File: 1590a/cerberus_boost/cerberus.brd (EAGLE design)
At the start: 33 x 31.7 mm, 30 parts, among them Q1 2N5088, Q2 2N5088, Q3 2N5087

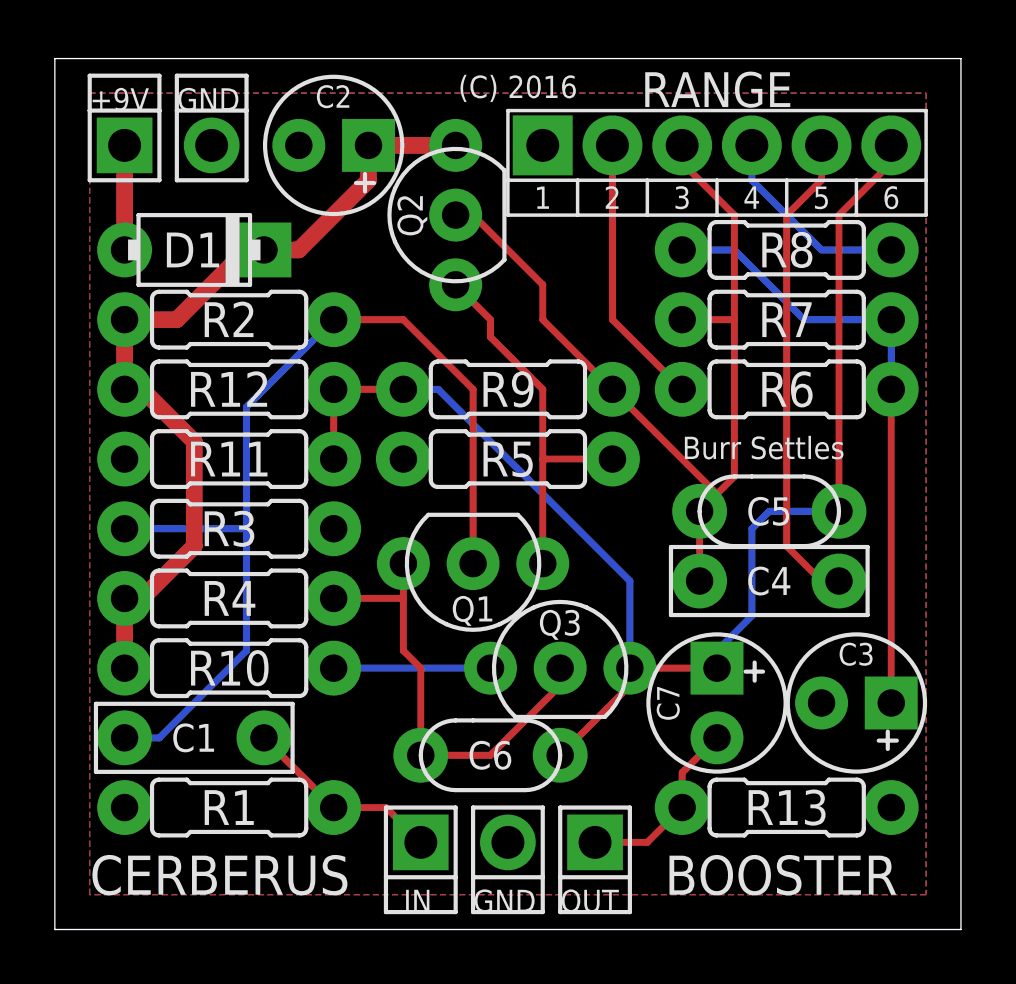
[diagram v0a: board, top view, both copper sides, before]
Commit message: prettified schematics a bit
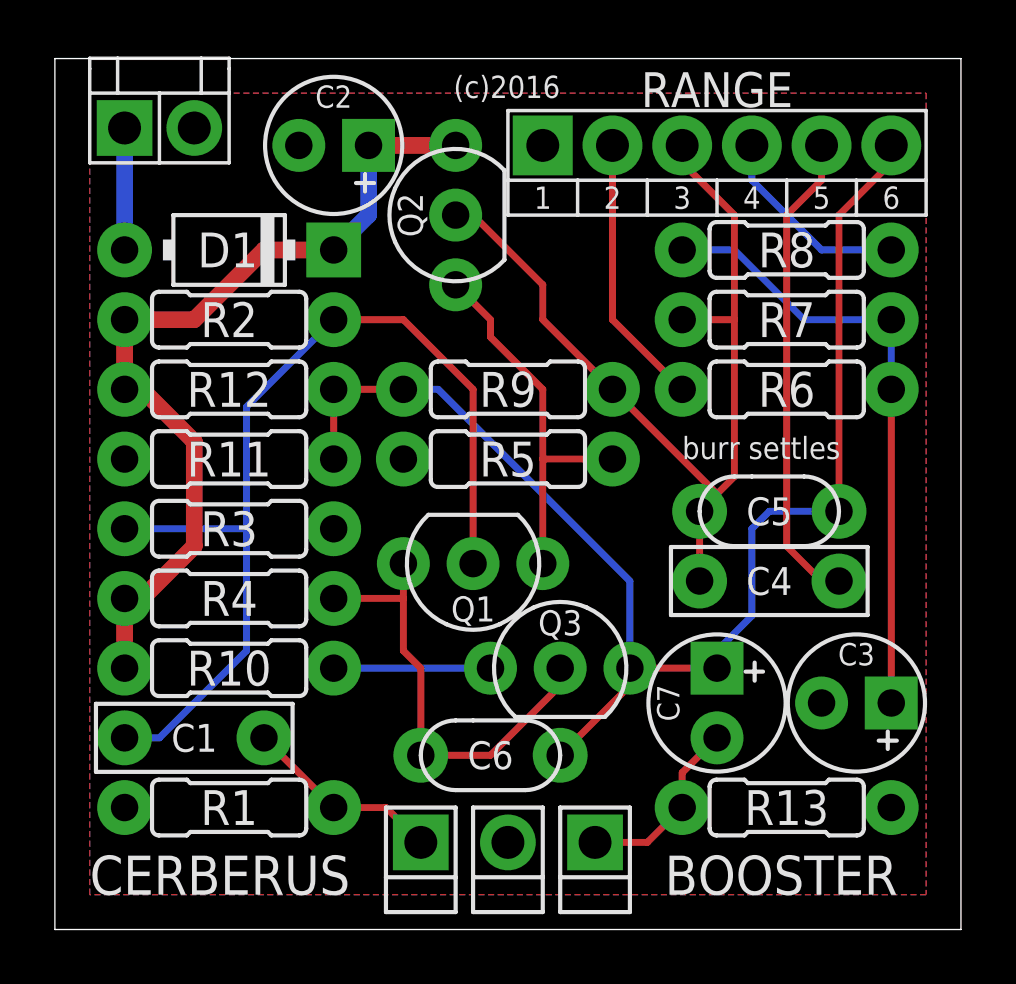
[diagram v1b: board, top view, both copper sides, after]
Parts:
- removed PAD1: PADSQR, supply pins:SQUARE
- removed PAD3: PADRND, supply pins:ROUND
- added 9V: DC_MONO, jacks:DC
- D1: device diodes:DO41-2 -> diodes:DO41-3
- moved D1 1.27 mm to (6.35, 24.8)
- renumbered PAD2 to IN, PAD4 to GND, PAD5 to OUT
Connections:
- removed net +9V: D1.A, PAD1.1
- new net N$3: 9V.T, D1.A
- net GND: now also 9V.S; no longer PAD3.1
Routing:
- net N$3: track 0.00 -> 4.45 mm
- net +9V: track 3.81 -> 0.00 mm
- net N$7: track 31.0 -> 31.7 mm
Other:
- board text added: "(c)2016"
- board text added: "burr settles"
- board text removed: "(C) 2016"
- board text removed: "+9V"
- board text removed: "Burr Settles"
- board text removed: "GND"
- board text removed: "IN"
- board text removed: "OUT"
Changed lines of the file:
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@@
 <drawing>
 <settings>
-<setting alwaysvectorfont="no"/>
+<setting alwaysvectorfont="yes"/>
 <setting verticaltext="up"/>
 </settings>
@@
 <wire x1="33.02" y1="31.74" x2="0" y2="31.74" width="0" layer="20"/>
 <wire x1="0" y1="31.74" x2="0" y2="0" width="0" layer="20"/>
-<text x="12.7" y="0.635" size="0.8128" layer="25" font="vector">IN</text>
-<text x="15.24" y="0.635" size="0.8128" layer="25" font="vector">GND</text>
-<text x="18.415" y="0.635" size="0.8128" layer="25" font="vector">OUT</text>
-<text x="4.445" y="29.845" size="0.8128" layer="25" font="vector">GND</text>
-<text x="1.27" y="29.845" size="0.8128" layer="25" font="vector">+9V</text>
 <text x="1.27" y="1.27" size="1.4224" layer="25" font="vector">CERBERUS</text>
 <text x="22.225" y="1.27" size="1.4224" layer="25" font="vector">BOOSTER</text>
-<text x="19.05" y="31.115" size="0.8128" layer="25" font="vector" rot="R180">(C) 2016</text>
-<text x="22.86" y="17.145" size="0.8128" layer="25" font="vector">Burr Settles</text>
+<text x="18.415" y="31.115" size="0.8128" layer="25" font="vector" rot="R180">(c)2016</text>
+<text x="22.86" y="17.145" size="0.8128" layer="25" font="vector">burr settles</text>
 </plain>
 <attributes>
@@
 <element name="C4" library="capacitors-film" package="BOX_SMALL" value="10n" x="26.035" y="12.7" rot="R180"/>
 <element name="C3" library="capacitors-elec" package="050_020_1" value="4u7" x="29.21" y="8.255" rot="R180"/>
-<element name="PAD5" library="supply pins" package="SQUARE" value="PADSQR" x="19.685" y="3.175"/>
-<element name="PAD2" library="supply pins" package="SQUARE" value="PADSQR" x="13.335" y="3.175"/>
-<element name="PAD1" library="supply pins" package="SQUARE" value="PADSQR" x="2.54" y="28.575" rot="R180"/>
-<element name="PAD3" library="supply pins" package="ROUND" value="PADRND" x="5.715" y="28.575" rot="R180"/>
-<element name="PAD4" library="supply pins" package="ROUND" value="PADRND" x="16.51" y="3.175"/>
+<element name="OUT" library="supply pins" package="SQUARE" value="PADSQR" x="19.685" y="3.175"/>
+<element name="IN" library="supply pins" package="SQUARE" value="PADSQR" x="13.335" y="3.175"/>
+<element name="GND" library="supply pins" package="ROUND" value="PADRND" x="16.51" y="3.175"/>
 <element name="Q1" library="transistors" package="TO92-" value="2N5088" x="15.24" y="13.335" rot="R180"/>
 <element name="Q2" library="transistors" package="TO92-" value="2N5088" x="14.605" y="26.035" rot="R90"/>
@@
 <element name="R1" library="resistors" package="R0207/3" value="1M" x="6.35" y="4.445"/>
 <element name="R13" library="resistors" package="R0207/3" value="2M2***" x="26.67" y="4.445" rot="R180"/>
-<element name="D1" library="diodes" package="DO41-2" value="1N5817" x="5.08" y="24.765" rot="R180"/>
+<element name="D1" library="diodes" package="DO41-3" value="1N5817" x="6.35" y="24.765" rot="R180"/>
+<element name="9V" library="jacks" package="DC" value="DC_MONO" x="3.81" y="29.21" rot="MR0"/>
 </elements>
 <signals>
-<signal name="IN">
-<contactref element="C1" pad="2"/>
-<contactref element="PAD2" pad="1"/>
-<contactref element="R1" pad="2"/>
-<wire x1="7.62" y1="6.985" x2="10.16" y2="4.445" width="0.254" layer="1"/>
-<wire x1="10.16" y1="4.445" x2="12.065" y2="4.445" width="0.254" layer="1"/>
-<wire x1="12.065" y1="4.445" x2="13.335" y2="3.175" width="0.254" layer="1"/>
-</signal>
 <signal name="N$1">
 <contactref element="Q1" pad="2"/>
@@
 <wire x1="15.24" y1="19.685" x2="12.7" y2="22.225" width="0.254" layer="1"/>
 <wire x1="12.7" y1="22.225" x2="10.16" y2="22.225" width="0.254" layer="1"/>
-</signal>
-<signal name="+9V">
-<contactref element="PAD1" pad="1"/>
-<contactref element="D1" pad="A"/>
-<wire x1="2.54" y1="28.575" x2="2.54" y2="24.765" width="0.6096" layer="1"/>
 </signal>
 <signal name="N$2">
@@
 <wire x1="20.955" y1="12.7" x2="20.955" y2="9.525" width="0.254" layer="16"/>
 </signal>
-<signal name="OUT">
-<contactref element="PAD5" pad="1"/>
-<contactref element="C7" pad="-"/>
-<contactref element="R13" pad="2"/>
-<wire x1="19.685" y1="3.175" x2="21.59" y2="3.175" width="0.254" layer="1"/>
-<wire x1="21.59" y1="3.175" x2="22.86" y2="4.445" width="0.254" layer="1"/>
-<wire x1="22.86" y1="4.445" x2="22.86" y2="5.715" width="0.254" layer="1"/>
-<wire x1="22.86" y1="5.715" x2="24.13" y2="6.985" width="0.254" layer="1"/>
-</signal>
 <signal name="N$10">
 <contactref element="RANGE" pad="P$3"/>
@@
 <signal name="GND">
 <contactref element="C2" pad="-"/>
-<contactref element="PAD4" pad="1"/>
+<contactref element="GND" pad="1"/>
 <contactref element="C3" pad="-"/>
 <polygon width="0.4064" layer="16">
@@
 <contactref element="R5" pad="1"/>
 <contactref element="R1" pad="1"/>
-<contactref element="PAD3" pad="1"/>
 <contactref element="R13" pad="1"/>
+<contactref element="9V" pad="S"/>
 </signal>
 <signal name="N$7">
@@
 <contactref element="Q2" pad="1"/>
 <contactref element="D1" pad="C"/>
-<wire x1="7.62" y1="24.765" x2="8.89" y2="24.765" width="0.6096" layer="1"/>
-<wire x1="8.89" y1="24.765" x2="11.43" y2="27.305" width="0.6096" layer="1"/>
-<wire x1="11.43" y1="27.305" x2="11.43" y2="28.575" width="0.6096" layer="1"/>
 <wire x1="11.43" y1="28.575" x2="14.605" y2="28.575" width="0.6096" layer="1"/>
-<wire x1="7.62" y1="24.765" x2="6.985" y2="24.765" width="0.6096" layer="1"/>
-<wire x1="6.985" y1="24.765" x2="4.445" y2="22.225" width="0.6096" layer="1"/>
-<wire x1="4.445" y1="22.225" x2="2.54" y2="22.225" width="0.6096" layer="1"/>
 <wire x1="2.54" y1="22.225" x2="2.54" y2="19.685" width="0.6096" layer="1"/>
 <wire x1="2.54" y1="19.685" x2="3.175" y2="19.685" width="0.6096" layer="1"/>
@@
 <wire x1="3.175" y1="12.065" x2="2.54" y2="12.065" width="0.6096" layer="1"/>
 <wire x1="2.54" y1="12.065" x2="2.54" y2="9.525" width="0.6096" layer="1"/>
+<wire x1="11.43" y1="28.575" x2="11.43" y2="26.035" width="0.6096" layer="16"/>
+<wire x1="11.43" y1="26.035" x2="10.16" y2="24.765" width="0.6096" layer="16"/>
+<wire x1="10.16" y1="24.765" x2="7.62" y2="24.765" width="0.6096" layer="1"/>
+<wire x1="7.62" y1="24.765" x2="5.08" y2="22.225" width="0.6096" layer="1"/>
+<wire x1="5.08" y1="22.225" x2="2.54" y2="22.225" width="0.6096" layer="1"/>
 </signal>
 <signal name="N$8">
@@
 <wire x1="27.94" y1="12.7" x2="28.575" y2="12.7" width="0.254" layer="1"/>
 </signal>
+<signal name="N$3">
+<contactref element="D1" pad="A"/>
+<contactref element="9V" pad="T"/>
+<wire x1="2.54" y1="29.21" x2="2.54" y2="24.765" width="0.6096" layer="16"/>
+</signal>
+<signal name="IN">
+<contactref element="C1" pad="2"/>
+<contactref element="IN" pad="1"/>
+<contactref element="R1" pad="2"/>
+<wire x1="7.62" y1="6.985" x2="10.16" y2="4.445" width="0.254" layer="1"/>
+<wire x1="10.16" y1="4.445" x2="12.065" y2="4.445" width="0.254" layer="1"/>
+<wire x1="12.065" y1="4.445" x2="13.335" y2="3.175" width="0.254" layer="1"/>
+</signal>
+<signal name="OUT">
+<contactref element="OUT" pad="1"/>
+<contactref element="C7" pad="-"/>
+<contactref element="R13" pad="2"/>
+<wire x1="19.685" y1="3.175" x2="21.59" y2="3.175" width="0.254" layer="1"/>
+<wire x1="21.59" y1="3.175" x2="22.86" y2="4.445" width="0.254" layer="1"/>
+<wire x1="22.86" y1="4.445" x2="22.86" y2="5.715" width="0.254" layer="1"/>
+<wire x1="22.86" y1="5.715" x2="24.13" y2="6.985" width="0.254" layer="1"/>
+</signal>
 </signals>

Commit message: added RT logo; converted some pots trimmers
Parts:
- added U$1: (no value), logos:RT150
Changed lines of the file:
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@@
 <element name="D1" library="diodes" package="DO41-3" value="1N5817" x="6.35" y="24.765" rot="R180"/>
 <element name="9V" library="jacks" package="DC" value="DC_MONO" x="3.81" y="29.21" rot="MR0"/>
+<element name="U$1" library="logos" package="RT150" value="" x="17.145" y="21.59"/>
 </elements>
 <signals>
@@
 <wire x1="27.305" y1="22.225" x2="30.48" y2="22.225" width="0.254" layer="16"/>
 <wire x1="30.48" y1="22.225" x2="30.48" y2="19.685" width="0.254" layer="16"/>
-<wire x1="30.48" y1="19.685" x2="30.48" y2="8.255" width="0.254" layer="1"/>
+<wire x1="30.48" y1="19.685" x2="30.48" y2="8.255" width="0.254" layer="16"/>
 </signal>
 <signal name="N$14">
@@
 <contactref element="C3" pad="-"/>
 <polygon width="0.4064" layer="16">
-<vertex x="1.27" y="30.48"/>
-<vertex x="31.75" y="30.48"/>
-<vertex x="31.75" y="1.27"/>
-<vertex x="1.27" y="1.27"/>
+<vertex x="0.635" y="31.115"/>
+<vertex x="32.385" y="31.115"/>
+<vertex x="32.385" y="0.635"/>
+<vertex x="0.635" y="0.635"/>
 </polygon>
 <polygon width="0.4064" layer="1">
-<vertex x="1.27" y="30.48"/>
-<vertex x="31.75" y="30.48"/>
-<vertex x="31.75" y="1.27"/>
-<vertex x="1.27" y="1.27"/>
+<vertex x="0.635" y="31.115"/>
+<vertex x="32.385" y="31.115"/>
+<vertex x="32.385" y="0.635"/>
+<vertex x="0.635" y="0.635"/>
 </polygon>
 <contactref element="R3" pad="1"/>

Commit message: updates to cerberus and cyclops
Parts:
- R13: value 2M2*** -> 1M
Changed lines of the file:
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@@
 <element name="RANGE" library="switches" package="DPDT_PADS" value="DPDT" x="24.13" y="28.575"/>
 <element name="R1" library="resistors" package="R0207/3" value="1M" x="6.35" y="4.445"/>
-<element name="R13" library="resistors" package="R0207/3" value="2M2***" x="26.67" y="4.445" rot="R180"/>
+<element name="R13" library="resistors" package="R0207/3" value="1M" x="26.67" y="4.445" rot="R180"/>
 <element name="D1" library="diodes" package="DO41-3" value="1N5817" x="6.35" y="24.765" rot="R180"/>
 <element name="9V" library="jacks" package="DC" value="DC_MONO" x="3.81" y="29.21" rot="MR0"/>

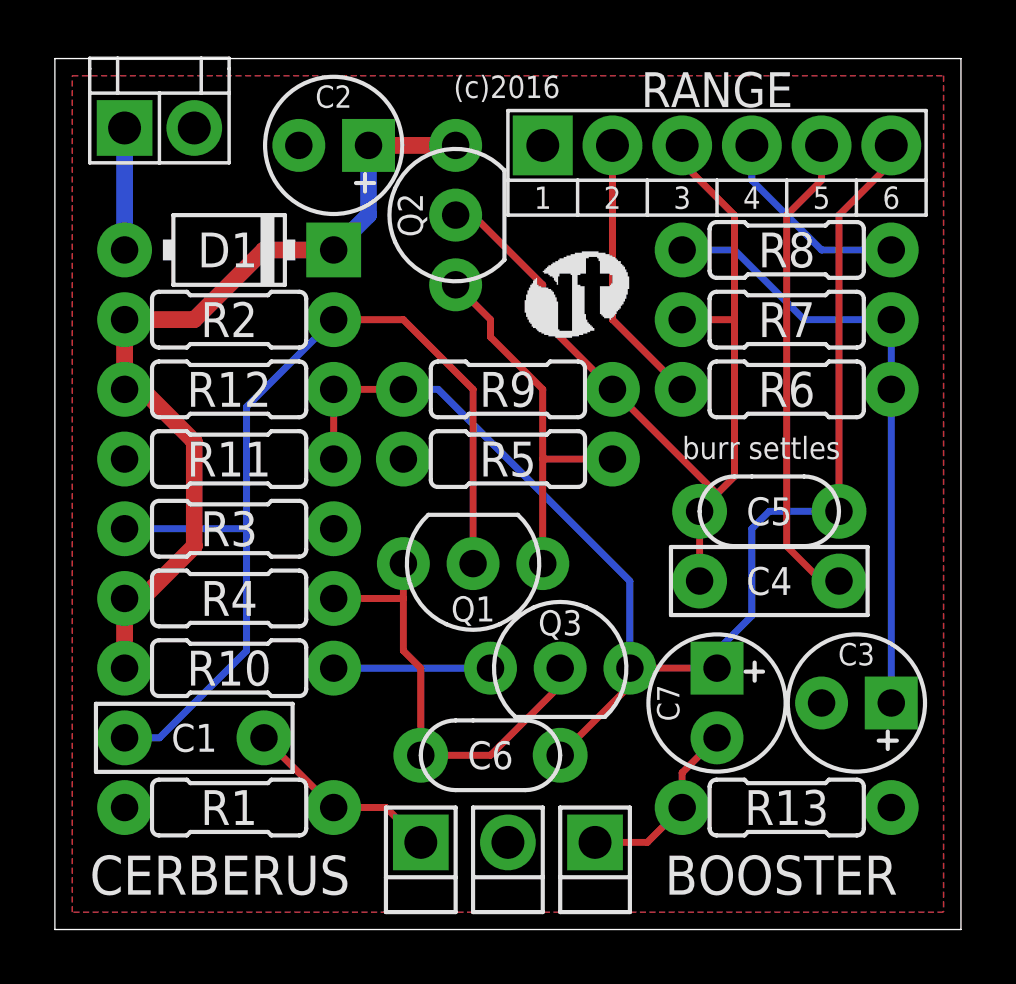
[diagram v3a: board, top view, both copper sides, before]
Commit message: convert bitmap logos to polygons
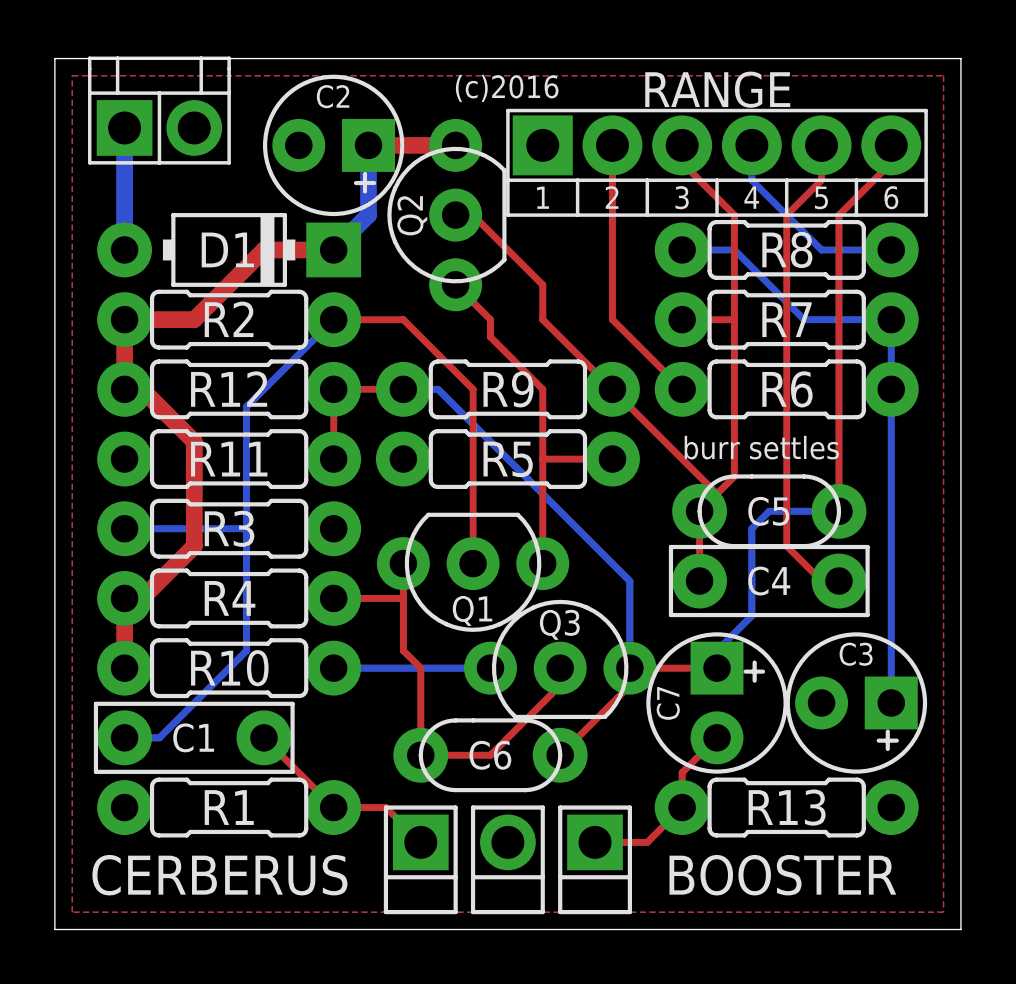
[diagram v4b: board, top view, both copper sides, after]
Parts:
- U$1: device logos:RT150 -> logos:RT0150
- moved U$1 2.69 mm to (19.1, 23.5)
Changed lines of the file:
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@@
 <element name="D1" library="diodes" package="DO41-3" value="1N5817" x="6.35" y="24.765" rot="R180"/>
 <element name="9V" library="jacks" package="DC" value="DC_MONO" x="3.81" y="29.21" rot="MR0"/>
-<element name="U$1" library="logos" package="RT150" value="" x="17.145" y="21.59"/>
+<element name="U$1" library="logos" package="RT0150" value="" x="19.05" y="23.495"/>
 </elements>
 <signals>
